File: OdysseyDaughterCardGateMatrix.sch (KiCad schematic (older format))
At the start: 17 parts, among them X1 OdysseyDaughterCard

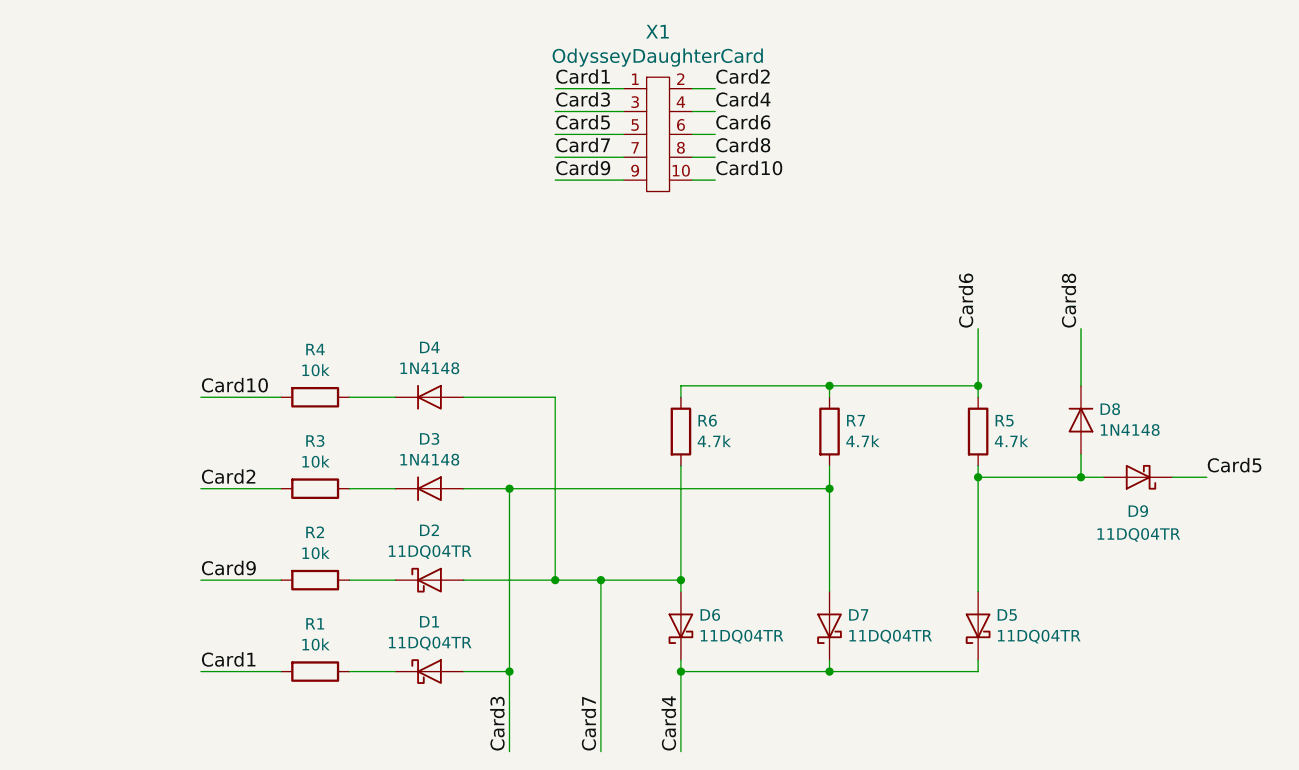
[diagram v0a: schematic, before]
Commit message: Fix component types in schematic
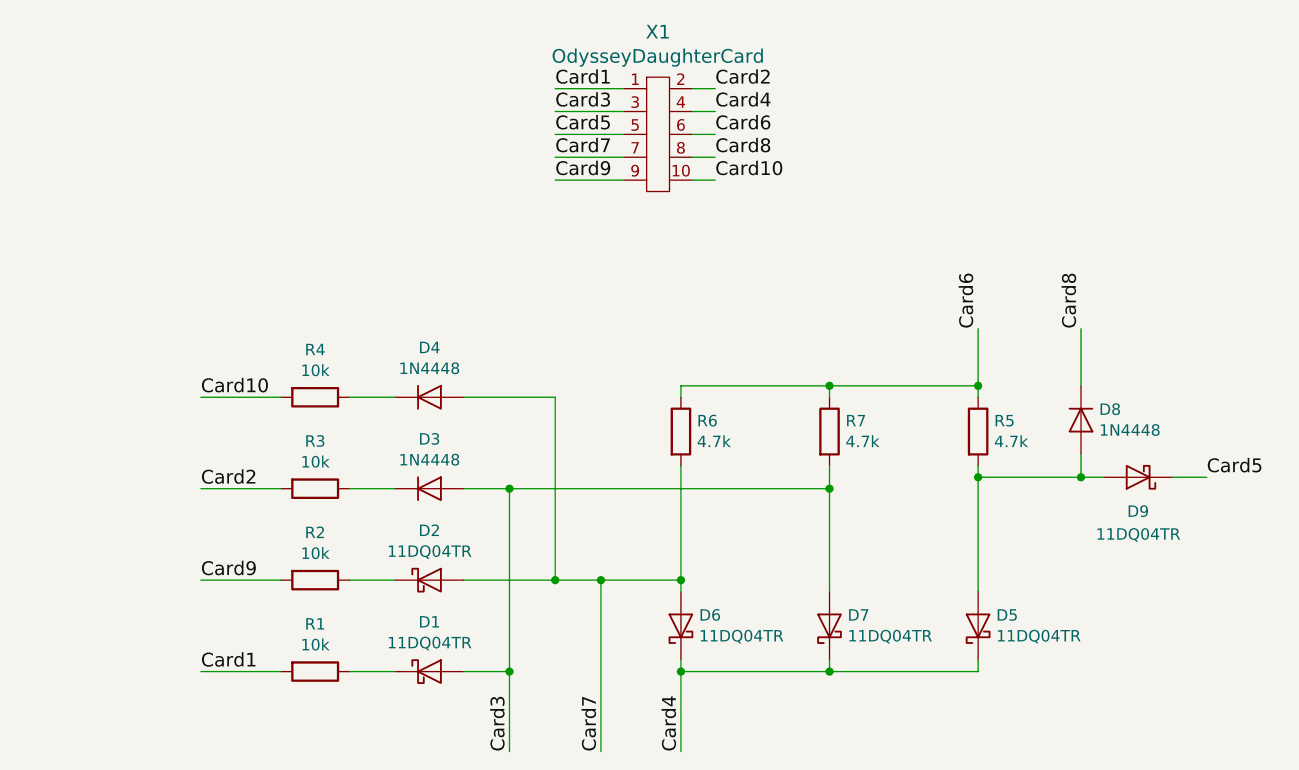
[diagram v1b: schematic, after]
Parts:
- D3, D4, D8: value 1N4148 -> 1N4448
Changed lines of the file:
@@
 P 4550 3450
 F 0 "D4" H 4550 3666 50  0000 C CNN
-F 1 "1N4148" H 4550 3575 50  0000 C CNN
+F 1 "1N4448" H 4550 3575 50  0000 C CNN
 F 2 "Diode_THT:D_DO-35_SOD27_P7.62mm_Horizontal" H 4550 3275 50  0001 C CNN
 F 3 "http://www.nxp.com/documents/data_sheet/1N4148_1N4448.pdf" H 4550 3450 50  0001 C CNN
@@
 P 4550 3850
 F 0 "D3" H 4550 4066 50  0000 C CNN
-F 1 "1N4148" H 4550 3975 50  0000 C CNN
+F 1 "1N4448" H 4550 3975 50  0000 C CNN
 F 2 "Diode_THT:D_DO-35_SOD27_P7.62mm_Horizontal" H 4550 3675 50  0001 C CNN
 F 3 "http://www.nxp.com/documents/data_sheet/1N4148_1N4448.pdf" H 4550 3850 50  0001 C CNN
@@
 P 7400 3550
 F 0 "D8" V 7354 3629 50  0000 L CNN
-F 1 "1N4148" V 7445 3629 50  0000 L CNN
+F 1 "1N4448" V 7445 3629 50  0000 L CNN
 F 2 "Diode_THT:D_DO-35_SOD27_P7.62mm_Horizontal" H 7400 3375 50  0001 C CNN
 F 3 "http://www.nxp.com/documents/data_sheet/1N4148_1N4448.pdf" H 7400 3550 50  0001 C CNN

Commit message: Change diode types, bump rev #
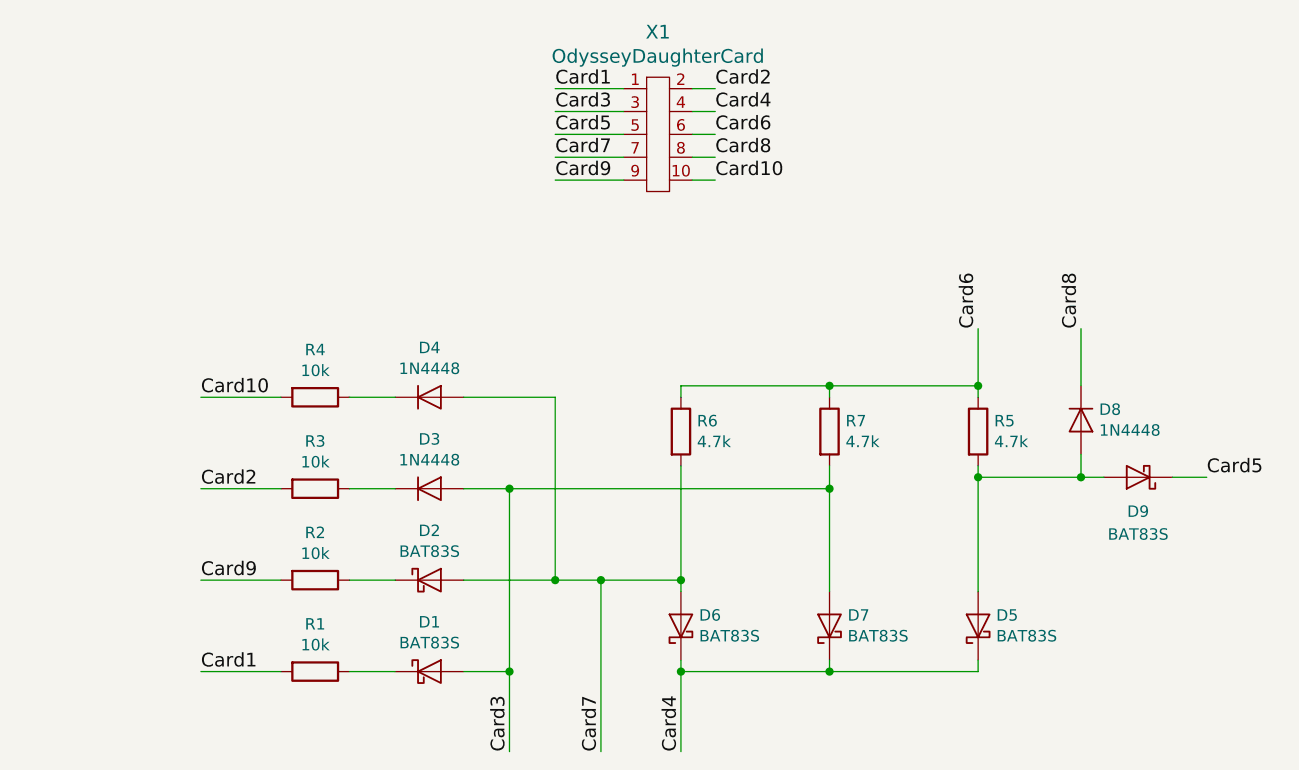
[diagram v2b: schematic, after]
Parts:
- D1, D2, D5, D6, D7, D9: value 11DQ04TR -> BAT83S
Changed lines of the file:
@@
 Sheet 1 1
 Title "Odyssey Daughter Card Gate Matrix"
-Date "2018-05-30"
-Rev "0.1"
+Date "2018-08-30"
+Rev "1.0"
 Comp "University of Pittsburgh - Odyssey Restoration Project"
 Comment1 "Levi Burner"
-Comment2 ""
+Comment2 "Derived from the scan of the original service manual made by David Winter"
 Comment3 ""
 Comment4 ""
@@
 P 4550 4250
 F 0 "D2" H 4550 4466 50  0000 C CNN
-F 1 "11DQ04TR" H 4550 4375 50  0000 C CNN
+F 1 "BAT83S" H 4550 4375 50  0000 C CNN
 F 2 "Diode_THT:D_DO-41_SOD81_P7.62mm_Horizontal" H 4550 4250 50  0001 C CNN
 F 3 "~" H 4550 4250 50  0001 C CNN
@@
 P 4550 4650
 F 0 "D1" H 4550 4866 50  0000 C CNN
-F 1 "11DQ04TR" H 4550 4775 50  0000 C CNN
+F 1 "BAT83S" H 4550 4775 50  0000 C CNN
 F 2 "Diode_THT:D_DO-41_SOD81_P7.62mm_Horizontal" H 4550 4650 50  0001 C CNN
 F 3 "~" H 4550 4650 50  0001 C CNN
@@
 P 5650 4450
 F 0 "D6" V 5696 4371 50  0000 R CNN
-F 1 "11DQ04TR" V 5605 4371 50  0000 R CNN
+F 1 "BAT83S" V 5605 4371 50  0000 R CNN
 F 2 "Diode_THT:D_DO-41_SOD81_P7.62mm_Horizontal" H 5650 4450 50  0001 C CNN
 F 3 "~" H 5650 4450 50  0001 C CNN
@@
 P 6300 4450
 F 0 "D7" V 6346 4371 50  0000 R CNN
-F 1 "11DQ04TR" V 6255 4371 50  0000 R CNN
+F 1 "BAT83S" V 6255 4371 50  0000 R CNN
 F 2 "Diode_THT:D_DO-41_SOD81_P7.62mm_Horizontal" H 6300 4450 50  0001 C CNN
 F 3 "~" H 6300 4450 50  0001 C CNN
@@
 P 6950 4450
 F 0 "D5" V 6996 4371 50  0000 R CNN
-F 1 "11DQ04TR" V 6905 4371 50  0000 R CNN
+F 1 "BAT83S" V 6905 4371 50  0000 R CNN
 F 2 "Diode_THT:D_DO-41_SOD81_P7.62mm_Horizontal" H 6950 4450 50  0001 C CNN
 F 3 "~" H 6950 4450 50  0001 C CNN
@@
 P 7650 3800
 F 0 "D9" H 7650 3950 50  0000 C CNN
-F 1 "11DQ04TR" H 7650 4050 50  0000 C CNN
+F 1 "BAT83S" H 7650 4050 50  0000 C CNN
 F 2 "Diode_THT:D_DO-41_SOD81_P7.62mm_Horizontal" H 7650 3800 50  0001 C CNN
 F 3 "~" H 7650 3800 50  0001 C CNN

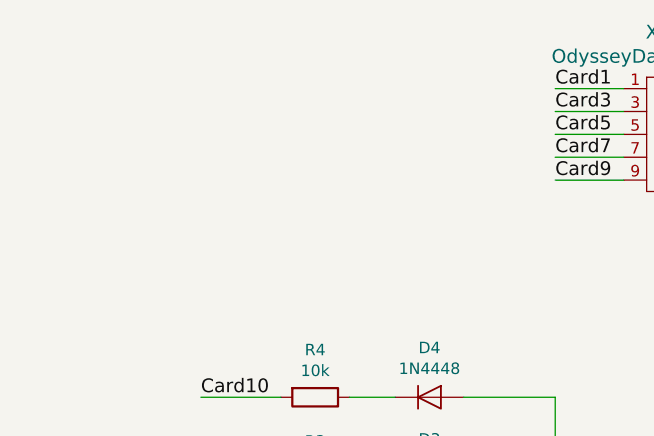
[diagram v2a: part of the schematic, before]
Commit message: R1.0 Add header for extra player generator
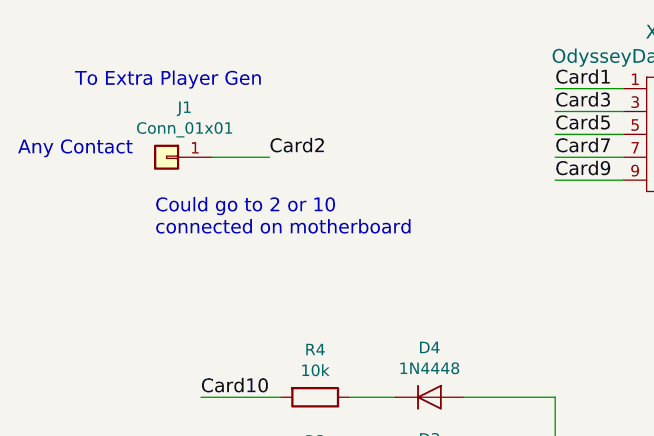
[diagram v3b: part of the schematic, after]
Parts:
- added J1: Conn_01x01, Connector_PinHeader_2.54mm:PinHeader_1x01_P2.54mm_Vertical, symbol Connector_Generic:Conn_01x01
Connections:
- net Card2: now also J1.1 (Pin_1)
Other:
- note added: "Any Contact"
- note added: "Could go to 2 or 10\nconnected on motherboard"
- note added: "To Extra Player Gen"
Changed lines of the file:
@@
 Sheet 1 1
 Title "Odyssey Daughter Card Gate Matrix"
-Date "2018-08-30"
+Date "2018-11-23"
 Rev "1.0"
 Comp "University of Pittsburgh - Odyssey Restoration Project"
@@
 Text Label 5100 2500 0    60   ~ 0
 Card9
+$Comp
+L Connector_Generic:Conn_01x01 J1
+U 1 1 5BFA52EE
+P 3400 2400
+F 0 "J1" H 3320 2617 50  0000 C CNN
+F 1 "Conn_01x01" H 3320 2526 50  0000 C CNN
+F 2 "Connector_PinHeader_2.54mm:PinHeader_1x01_P2.54mm_Vertical" H 3400 2400 50  0001 C CNN
+F 3 "~" H 3400 2400 50  0001 C CNN
+	1    3400 2400
+	-1   0    0    -1
+$EndComp
+Text Notes 3000 2100 0    60   ~ 0
+To Extra Player Gen
+Text Notes 2750 2400 0    60   ~ 0
+Any Contact
+Wire Wire Line
+	3600 2400 3850 2400
+Text Label 3850 2400 0    60   ~ 0
+Card2
+Text Notes 3350 2750 0    60   ~ 0
+Could go to 2 or 10\nconnected on motherboard
 $EndSCHEMATC
